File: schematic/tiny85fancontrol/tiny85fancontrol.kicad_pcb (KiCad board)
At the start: 2 copper layers, 25.4 x 25.4 mm, 11 parts, among them J1 UART_DBG, J2 Molex, M1 Fan, Q1 IRF3808, U1 ATtiny85-20P, U2 DS18B20

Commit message: Fix: Temperature sensor connected backwards
Thanks to amdj at #kicad for spotting this issue
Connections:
- U2 pad 1: +5V -> GND
- U2 pad 3: GND -> +5V
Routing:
- net +5V: track 3.26 -> 0.00 mm
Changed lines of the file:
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@@
 			(layers "*.Cu" "*.Mask")
 			(remove_unused_layers no)
-			(net 2 "+5V")
+			(net 1 "GND")
 			(pinfunction "GND")
 			(pintype "power_in")
@@
 			(layers "*.Cu" "*.Mask")
 			(remove_unused_layers no)
-			(net 1 "GND")
+			(net 2 "+5V")
 			(pinfunction "V_{DD}")
 			(pintype "power_in")
@@
 		)
 	)
-	(segment
-		(start 43.923603 46.4)
-		(end 42.5 46.4)
-		(width 1)
-		(layer "B.Cu")
-		(net 2)
-	)
-	(segment
-		(start 45.01 45.95)
-		(end 45.46 45.5)
-		(width 1)
-		(layer "B.Cu")
-		(net 2)
-	)
-	(arc
-		(start 43.923603 46.4)
-		(mid 44.511556 46.283048)
-		(end 45.01 45.95)
-		(width 1)
-		(layer "B.Cu")
-		(net 2)
-	)
 	(arc
 		(start 33.69725 44.23725)
@@
 		(polygon
 			(pts
-				(xy 28.5 29.5) (xy 28.5 57.5) (xy 35.5 57.5) (xy 35.5 57.5) (xy 35.5 37) (xy 34 36) (xy 34 29.5)
+				(xy 28.5 29.5) (xy 28.5 57.5) (xy 35.5 57.5) (xy 35.5 37) (xy 34 36) (xy 34 29.5)
 			)
 		)

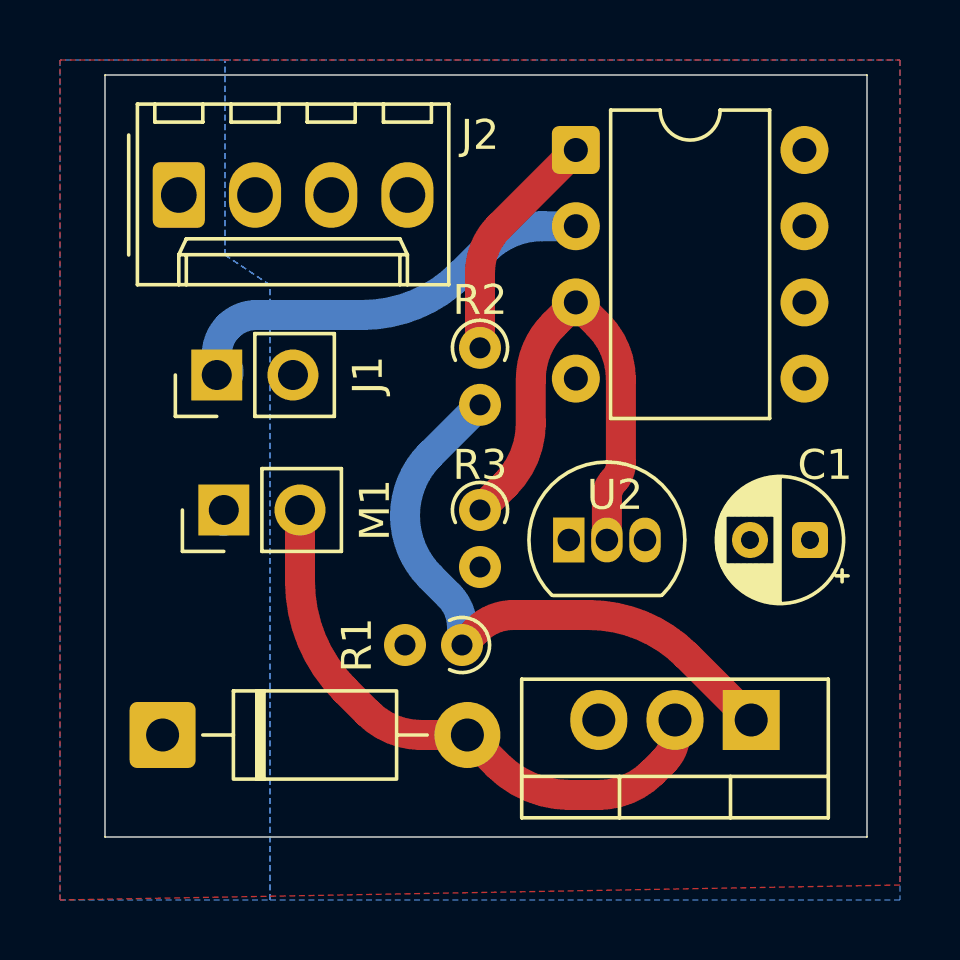
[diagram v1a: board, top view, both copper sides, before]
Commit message: Update Schematic and PCB According to Reviews
Placed temperature sensor away from MOSFET.
Fixed PIN assignments according to software.
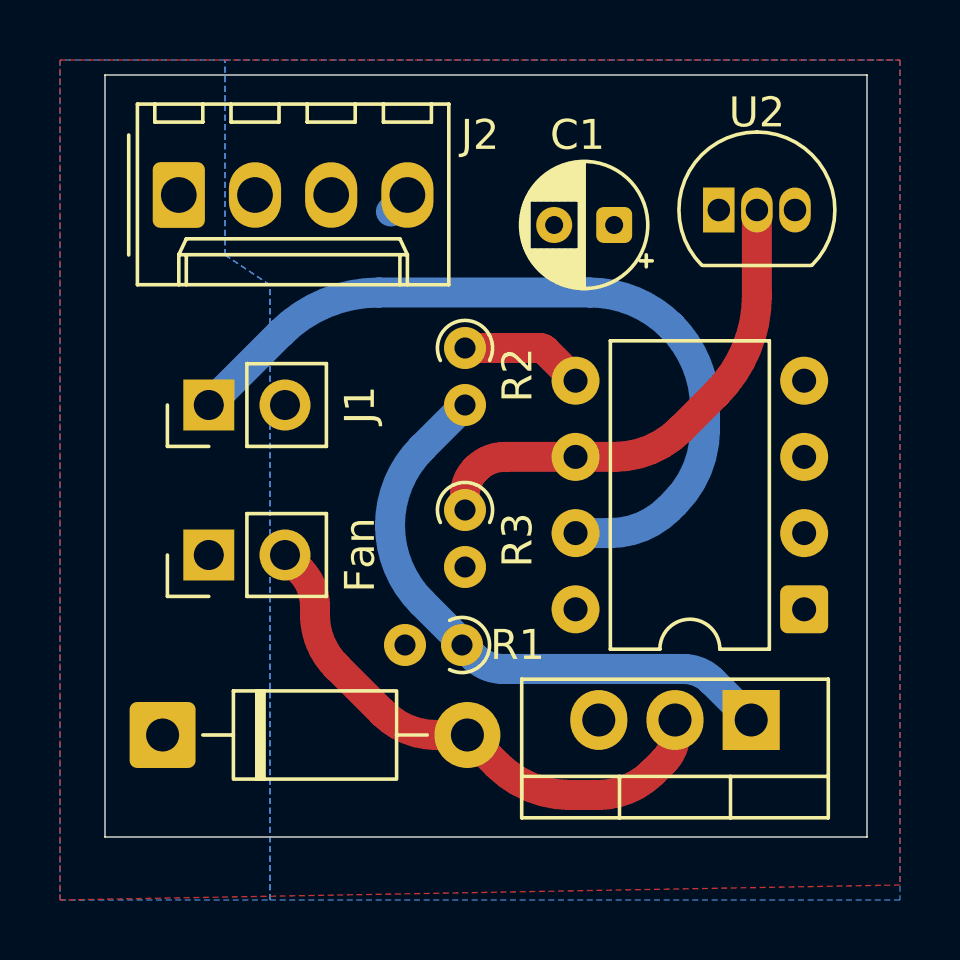
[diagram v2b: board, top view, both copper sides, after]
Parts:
- moved U1 17.1 mm to (53.3, 47.8), turned to 180 degrees
- moved C1 12.4 mm to (47.0, 35.0)
- moved U2 12.1 mm to (50.5, 34.5)
- moved M1 1.58 mm to (33.5, 46.0)
- moved J1 1.03 mm to (33.5, 41.0)
- moved R2 0.50 mm to (42.0, 39.1)
- moved R3 0.50 mm to (42.0, 44.5)
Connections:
- U1 pad 1: /PWM_SIGNAL -> unconnected-(U1-~{RESET}/PB5-Pad1)
- U1 pad 2: /UART_DEBUG_TX -> unconnected-(U1-XTAL1/PB3-Pad2)
- U1 pad 3: /TEMPERATURE_SIGNAL -> unconnected-(U1-XTAL2/PB4-Pad3)
- U1 pad 5: unconnected-(U1-AREF/PB0-Pad5) -> /PWM_SIGNAL
- U1 pad 6: unconnected-(U1-PB1-Pad6) -> /TEMPERATURE_SIGNAL
- U1 pad 7: unconnected-(U1-PB2-Pad7) -> /UART_DEBUG_TX
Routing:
- net /UART_DEBUG_TX: track 14.5 -> 27.0 mm
- net /PWM_SIGNAL: track 7.81 -> 4.12 mm
- net Net-(D1-A): track 19.5 -> 18.4 mm
- net +5V: track 0.00 -> 0.78 mm
- net +12V: track 0.70 -> 0.00 mm
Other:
- board text added: "REV1A"
